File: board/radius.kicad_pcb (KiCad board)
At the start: 2 copper layers, 26.3 x 27.6 mm, 11 parts, among them IC1 STM8S003F3P, P1 CONN_01X04, P2 CONN_01X10, U1 CH340G, U2 LM2931AZ-3.3/5.0, Y1 Crystal

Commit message: Updates Capacitor values.
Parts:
- C1: value C -> 0.1 µF
- C2: value C -> 100 nF
- C3: value C -> 1 μF
- C4, C5: value C -> 20 pF

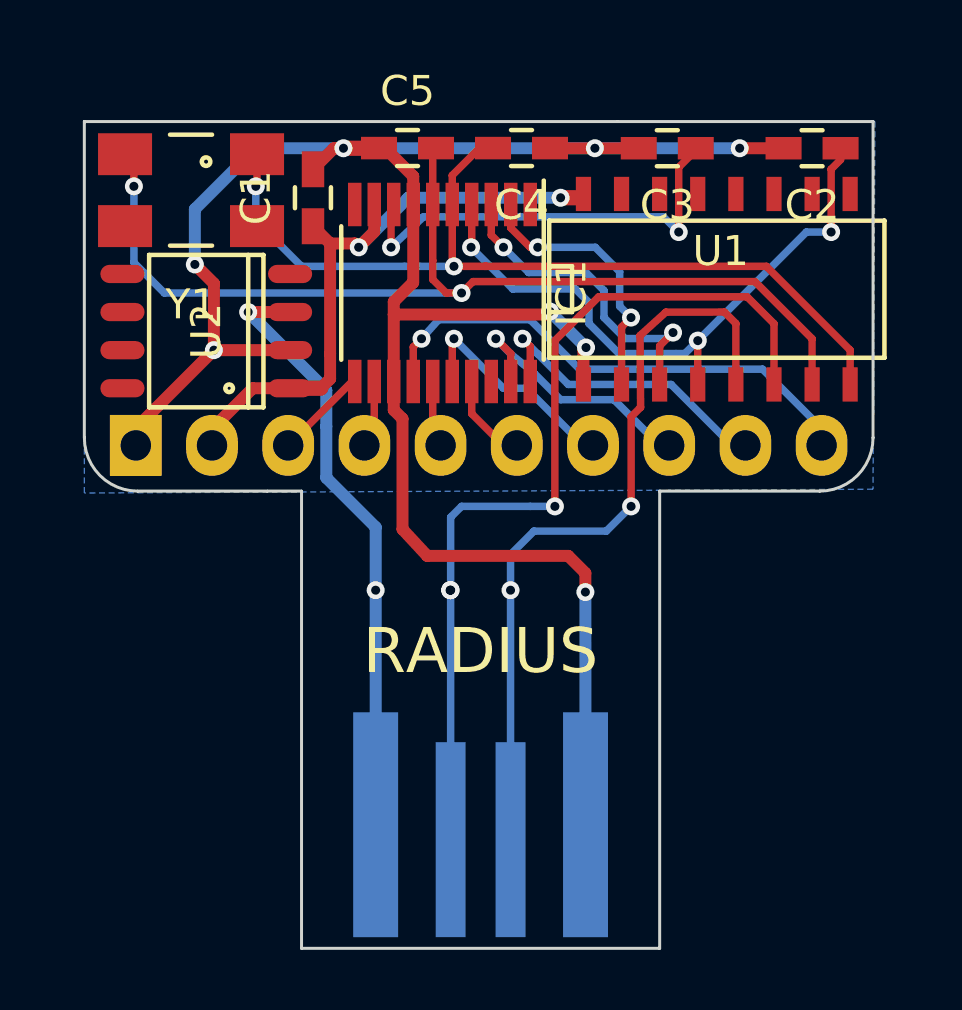
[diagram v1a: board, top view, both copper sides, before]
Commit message: Widens board to 1.1"
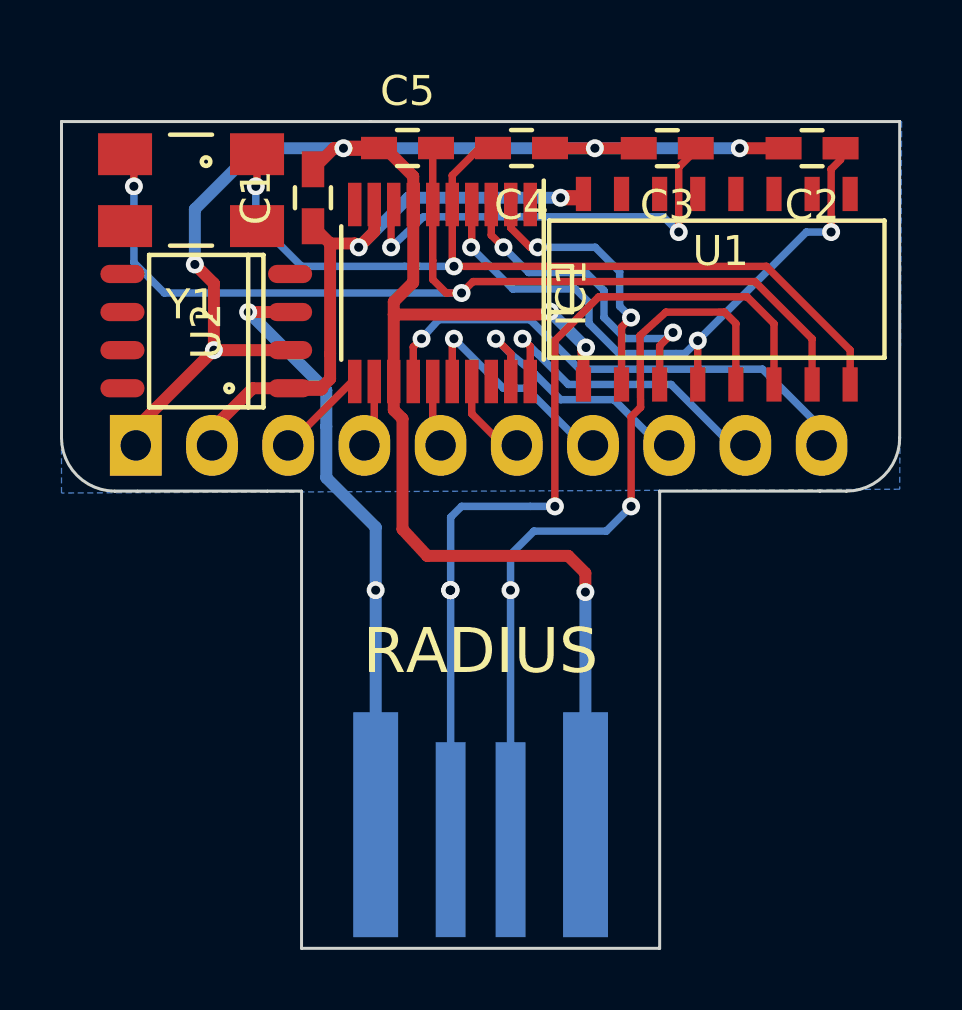
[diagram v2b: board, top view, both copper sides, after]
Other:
- board size 26.3 x 27.6 mm -> 27.9 x 27.6 mm

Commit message: Support SWIM connector.
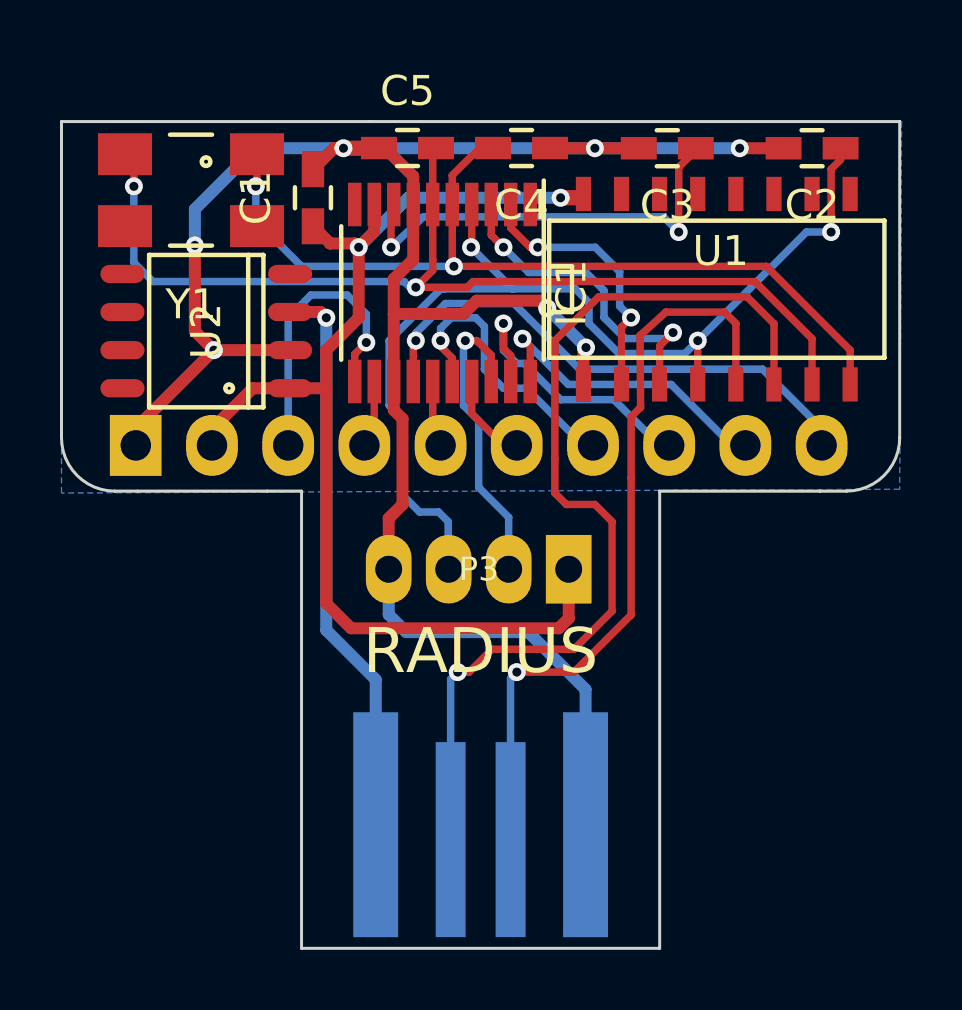
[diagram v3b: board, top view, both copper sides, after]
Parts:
- added P3: CONN_01X04, radius:RADIUS-CONN-2MM-M-1x4, F.Cu at (167.3, 119.2)
- C1: value 0.1 µF -> 10 µF
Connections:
- net Net-(C2-Pad1) renamed RST
- IC1 pad 18: (no net) -> SWIM
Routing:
- net VCC: track 21.9 -> 39.7 mm
- net RST: track 21.4 -> 35.0 mm
- net SWIM: track 0.00 -> 10.2 mm, vias 0 -> 1
- net SDA: track 3.10 -> 9.93 mm, vias 0 -> 1
- net MOSI: track 7.56 -> 9.75 mm
- net D-: track 30.2 -> 32.3 mm, vias 3 -> 1
- net +5V: track 20.2 -> 18.9 mm, vias 2 -> 1
- net TXD: track 8.87 -> 9.76 mm
- net XI: track 35.0 -> 34.2 mm
- net G3: track 17.3 -> 17.9 mm
- net GND: track 75.2 -> 75.6 mm, vias 8 -> 7
- net D+: track 26.0 -> 25.7 mm, vias 2 -> 1

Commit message: Corrects power adapter pinout.
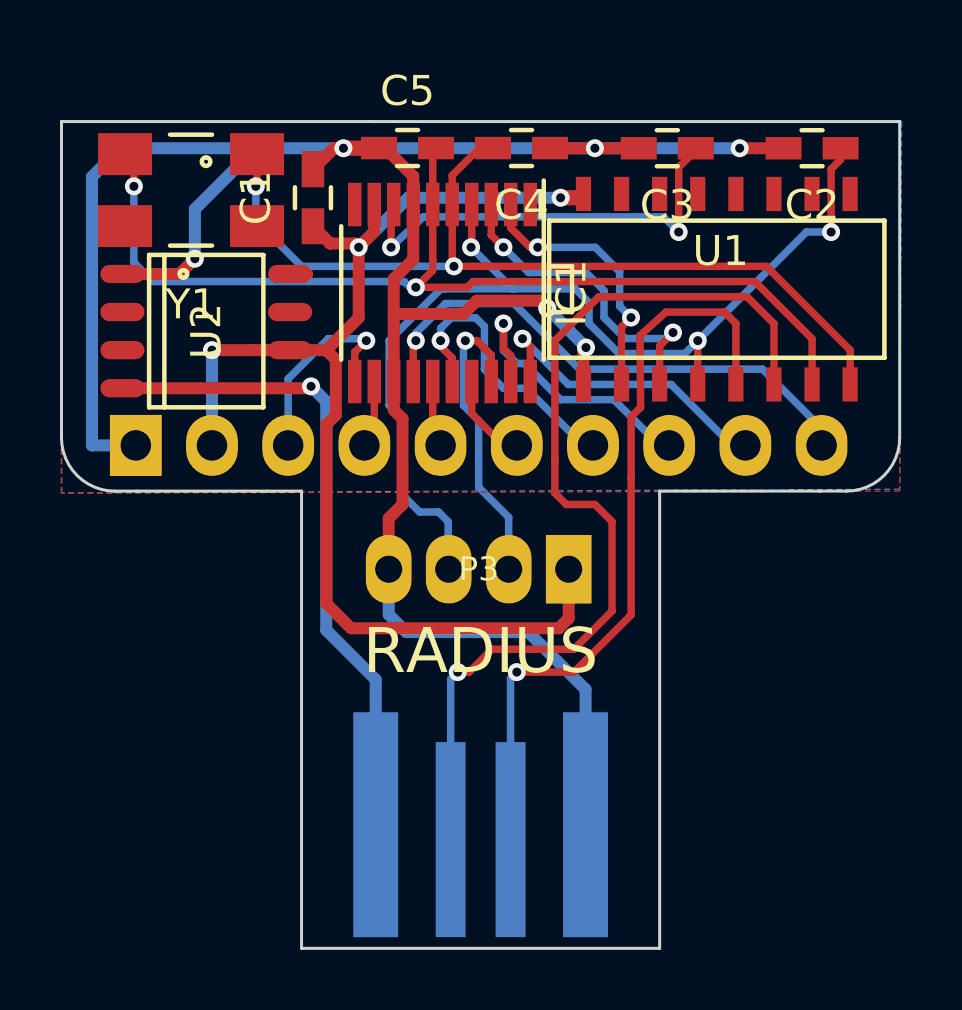
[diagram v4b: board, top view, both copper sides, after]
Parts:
- U2: value LM2931AZ-3.3/5.0 -> LD1117
- turned U2 to 270 degrees
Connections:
- U2 pad 1: VCC -> GND
- U2 pad 2: GND -> (no net)
- U2 pad 3: +5V -> (no net)
- U2 pad 4: (no net) -> +5V
- U2 pad 6: (no net) -> VCC
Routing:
- net GND: track 75.6 -> 84.4 mm, vias 7 -> 6
- net +5V: track 18.9 -> 21.8 mm
- net SDA: track 9.93 -> 7.02 mm
- net VCC: track 39.7 -> 41.6 mm, vias 2 -> 3
- net (no net): track 0.00 -> 0.57 mm
- added copper zone on F.Cu, net GND
